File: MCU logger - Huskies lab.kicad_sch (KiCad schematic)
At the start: 25 parts

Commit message: test changes
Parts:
- gave numbers to parts that had none: 25
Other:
- moved on the sheet: BT1, C1, U1, U2, U3, U4, Y1, Y2

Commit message: values of the componenents added.
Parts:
- C1: value C_Polarized -> 100nF
- C2: value C -> 0.1UF
- C3, C5: value C -> 22pF
- C4: value C -> 0.1pF
- R1, R3: value R -> 10k
- R2: value R -> 10K
- R4, R5: value R -> 4.7k
- R6, R7: value R -> 330
- Y1: value Crystal -> 32.768KHz
- Y2: value Crystal -> 16Mhz
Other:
- moved on the sheet: C2, C3, C4, C5, R1, R2

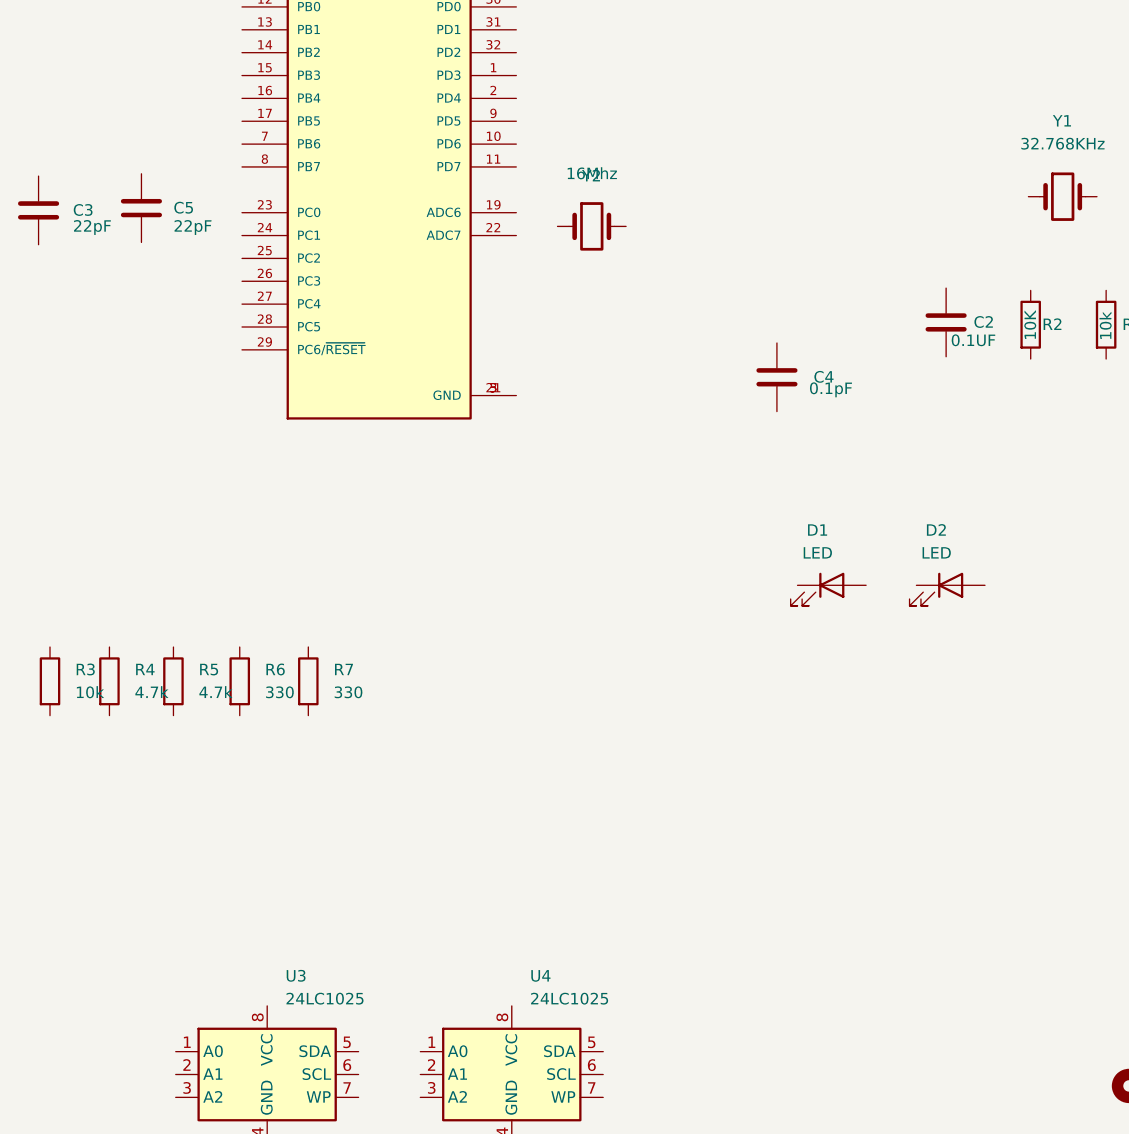
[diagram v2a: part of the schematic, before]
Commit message: added the symbols anb the footprints to every component
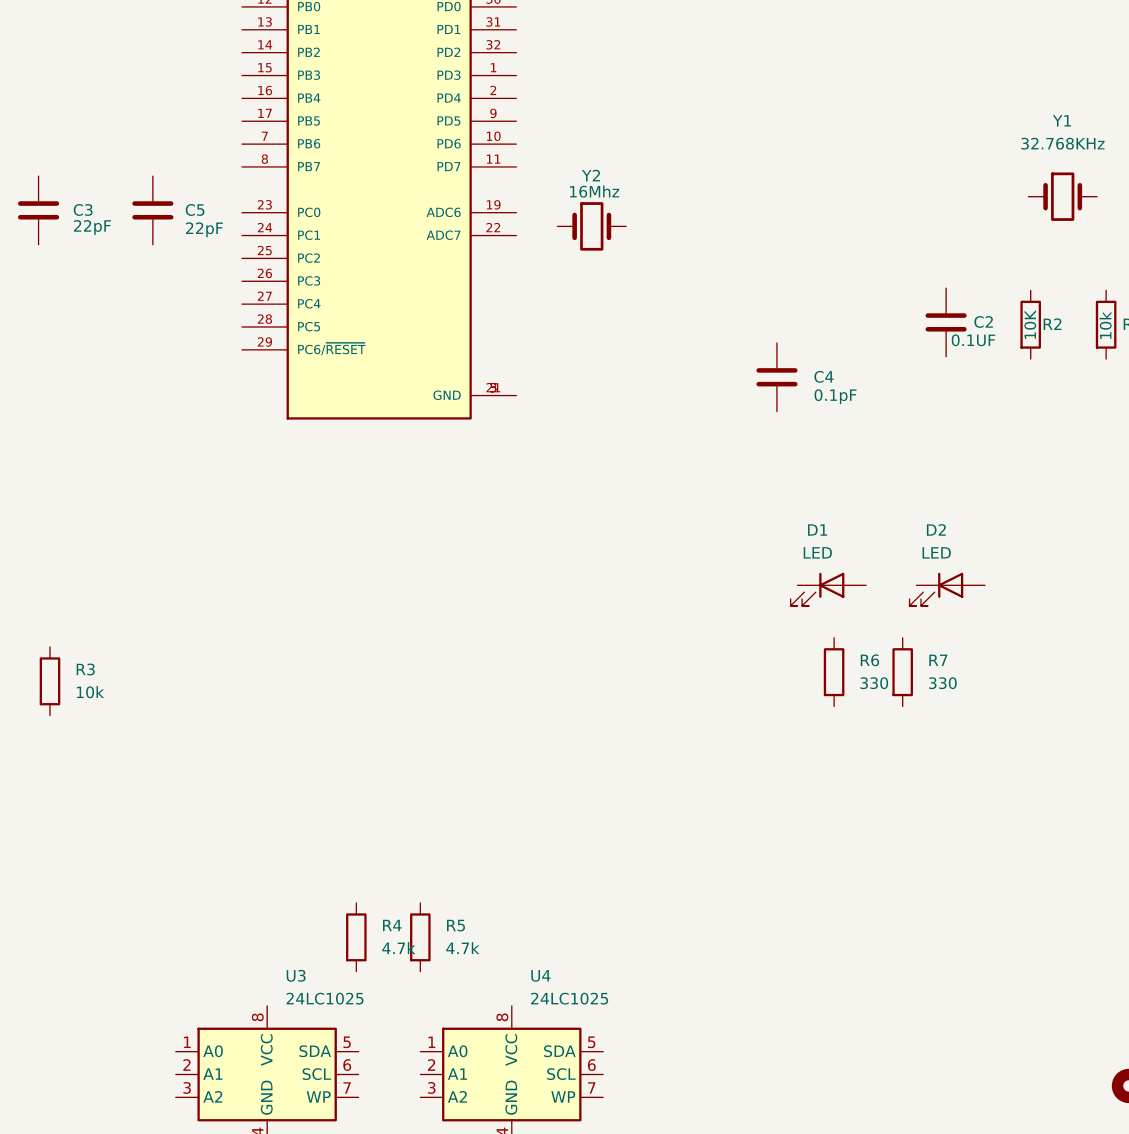
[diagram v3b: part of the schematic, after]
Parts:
- BT1: footprint (none) -> Connector_PinHeader_2.54mm:PinHeader_1x02_P2.54mm_Vertical
- C1, C2, C3, C4, C5: footprint (none) -> Capacitor_SMD:C_0805_2012Metric
- D1, D2: footprint (none) -> LED_SMD:LED_0805_2012Metric
- H1, H2, H3, H4: footprint (none) -> MountingHole:MountingHole_2.1mm
- R1, R2, R3, R4, R5, R6, R7: footprint (none) -> Resistor_SMD:R_0805_2012Metric_Pad1.20x1.40mm_HandSolder
- U1: footprint QFP80P900X900X120-32N -> footprints:QFP80P900X900X120-32N
- U2: footprint SOIC127P600X175-8N -> footprints:SOIC127P600X175-8N
- U3, U4: footprint (none) -> Package_SO:SOIC-8_5.23x5.23mm_P1.27mm
- Y1, Y2: footprint (none) -> Crystal:Crystal_HC49-U_Vertical
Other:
- moved on the sheet: C5, R4, R5, R6, R7

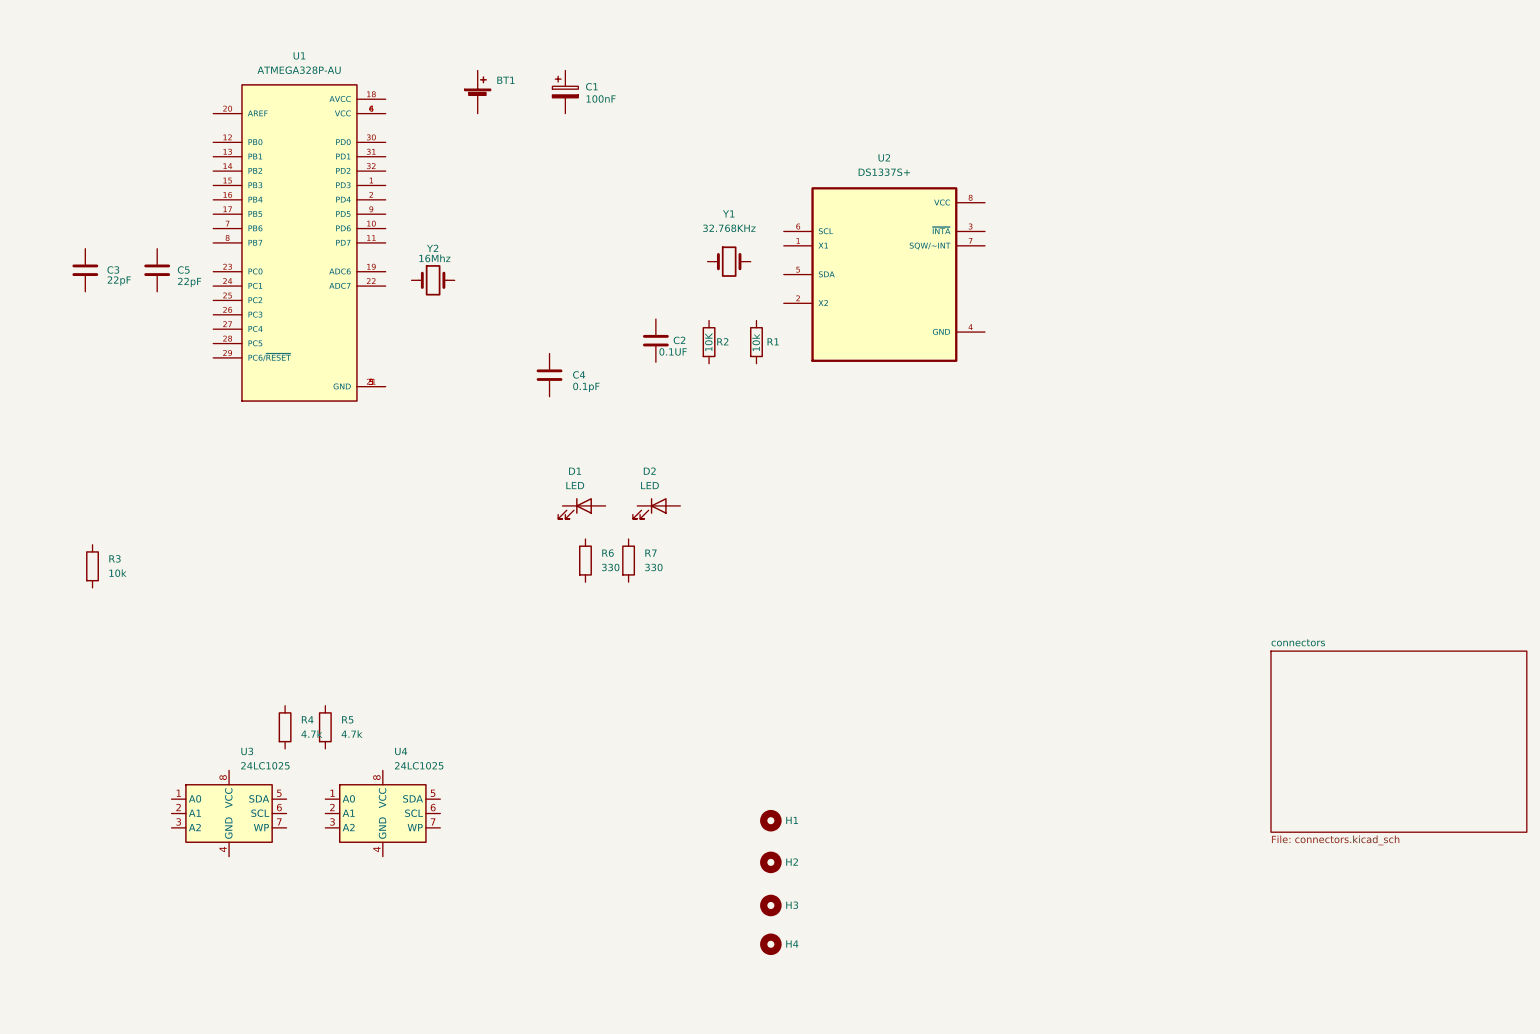
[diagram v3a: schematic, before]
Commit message: wiring of clock and EEPROM
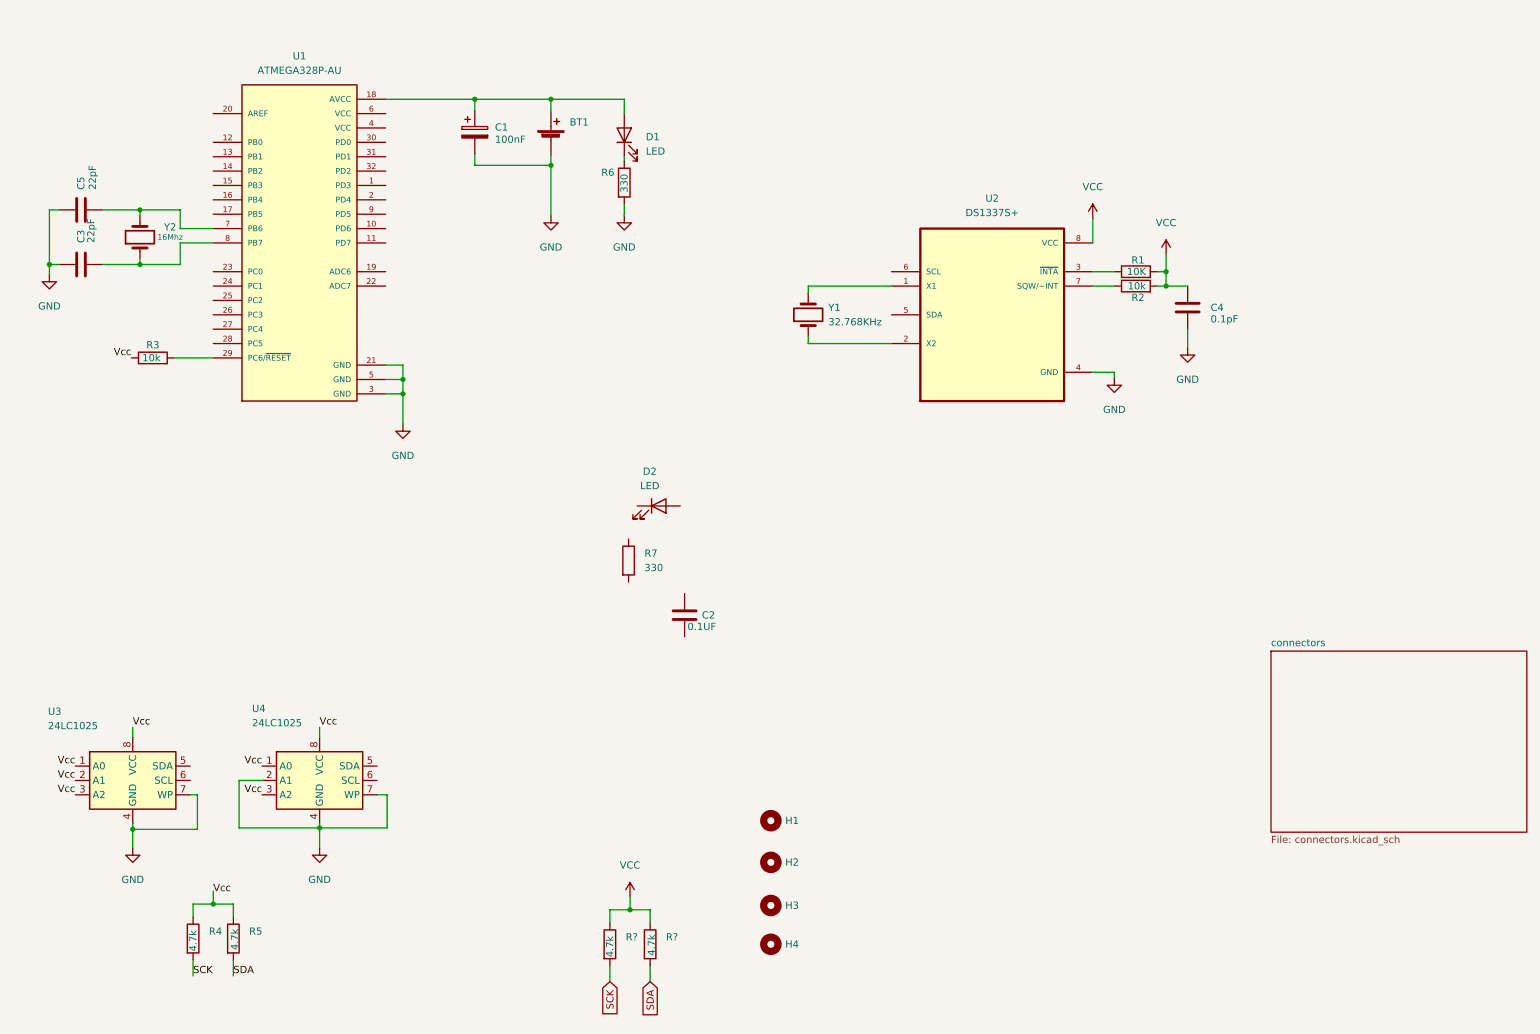
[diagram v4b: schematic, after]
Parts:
- added R? (x2): 4.7k, Resistor_SMD:R_0805_2012Metric_Pad1.20x1.40mm_HandSolder, symbol Device:R
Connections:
- net at Y2.1: now also C3.2, U1.8 (PB7)
- net at Y2.2: now also C5.2, U1.7 (PB6)
- net GND: now reaches C3.1
- net GND: now also BT1.2 (-), C1.2, C4.2, C5.1, R6.2, U1.21 (GND), U1.3 (GND), U1.5 (GND), U2.4 (GND), U3.4 (GND), U3.7 (WP), U4.2 (A1), U4.4 (GND), U4.7 (WP)
- net Vcc: now reaches U4.1 (A0)
- net Vcc: now also R3.1, R4.1, R5.1, U3.1 (A0), U3.2 (A1), U3.3 (A2), U3.8 (VCC), U4.3 (A2), U4.8 (VCC)
- net at BT1.1 (+): now also C1.1, D1.2 (A), U1.18 (AVCC)
- net at U1.29 (PC6/~{RESET}): now also R3.2
- net at U1.4 (VCC): no longer U1.6 (VCC)
- net VCC: now reaches C4.1
- net VCC: now also R1.2, R2.2, U2.8 (VCC), R?.1, R?.1
- net at R1.1: now also U2.7 (SQW/~INT)
- net SCK: now reaches R4.2
- net SCK: now also R?.2
- net at U2.1 (X1): now also Y1.2
- net at U2.2 (X2): now also Y1.1
- net at U2.3 (~{INTA}): now also R2.1
- net SDA: now reaches R5.2
- net SDA: now also R?.2
- net at R6.1: now also D1.1 (K)
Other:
- moved on the sheet: BT1, C1, C2, C3, C4, C5, D1, R1, R2, R3, R4, R5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

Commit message: wiring of the first sheet completed
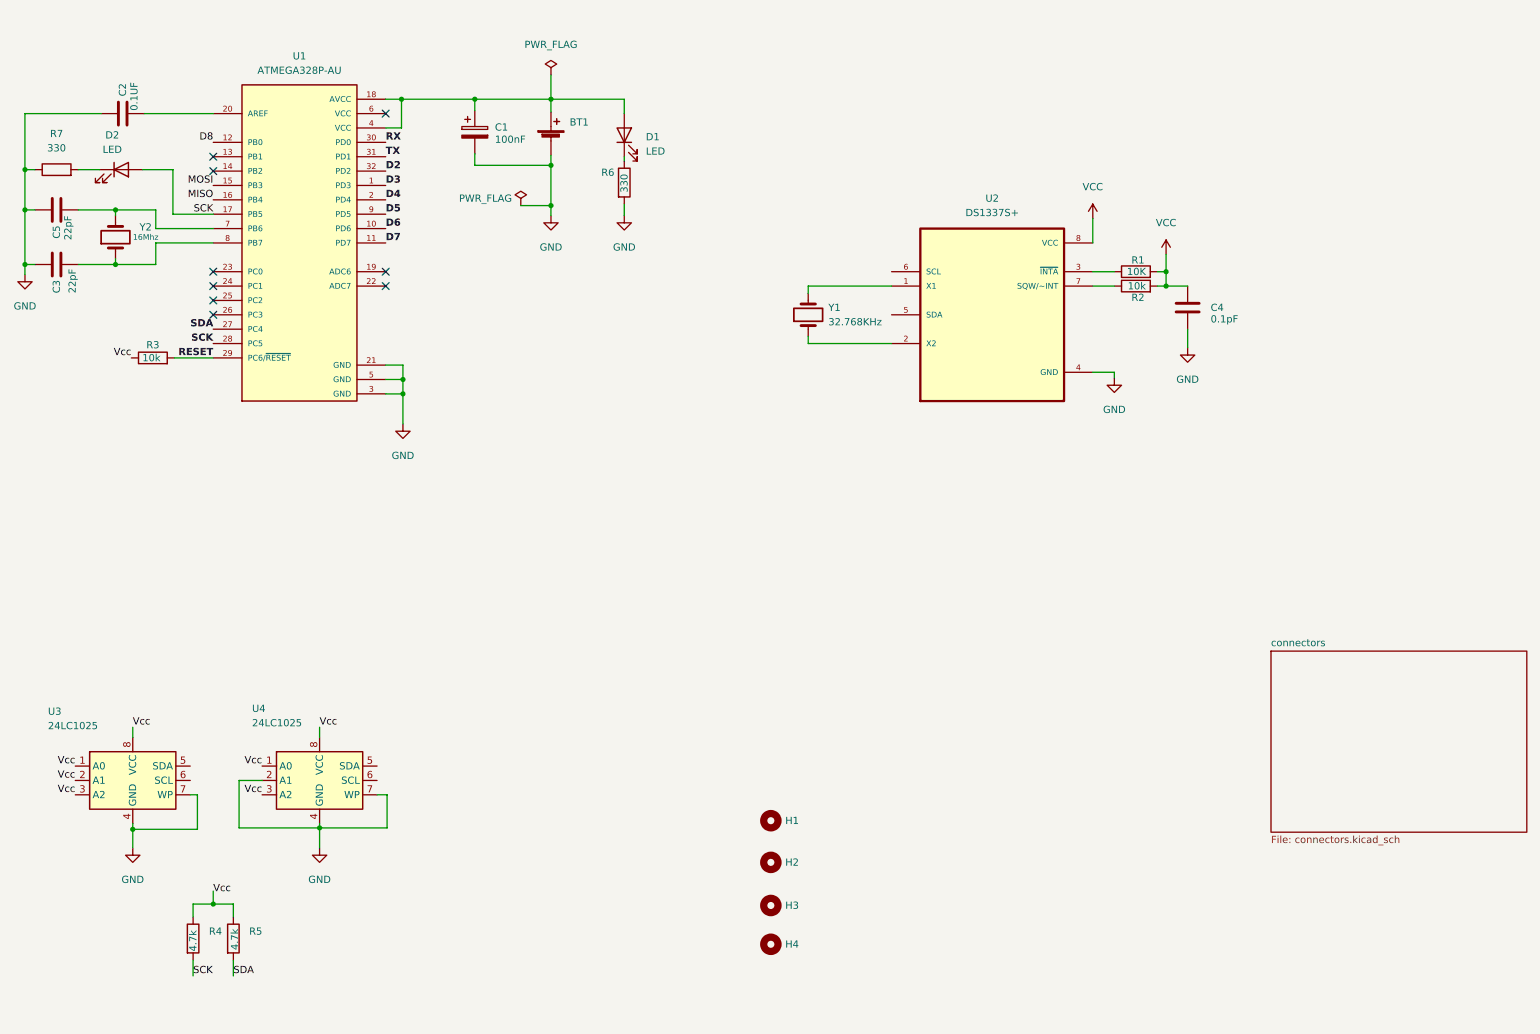
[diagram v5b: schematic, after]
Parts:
- removed R? (x2): 4.7k, Resistor_SMD:R_0805_2012Metric_Pad1.20x1.40mm_HandSolder, symbol Device:R
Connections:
- net GND: now also C2.1, R7.1
- net SCK: now also D2.2 (A), U1.17 (PB5), U1.28 (PC5)
- net SDA: now also U1.27 (PC4)
- net at D2.1 (K): now also R7.2
- net at BT1.1 (+), C1.1, D1.2 (A)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: now also U1.4 (VCC)
- net D3: now reaches U1.1 (PD3)
- net D6: now reaches U1.10 (PD6)
- net D7: now reaches U1.11 (PD7)
- net D8: now reaches U1.12 (PB0)
- net MOSI: now reaches U1.15 (PB3)
- net MISO: now reaches U1.16 (PB4)
- net D4: now reaches U1.2 (PD4)
- net at U1.20 (AREF): now also C2.2
- net RESET: now reaches R3.2, U1.29 (PC6/~{RESET})
- net RX: now reaches U1.30 (PD0)
- net TX: now reaches U1.31 (PD1)
- net D2: now reaches U1.32 (PD2)
- net D5: now reaches U1.9 (PD5)
- no-connect marks 0 -> 9
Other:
- moved on the sheet: C2, C3, C5, D2, R7, Y2
